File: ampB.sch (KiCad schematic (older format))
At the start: 14 parts, among them U05 Mux, U2 screw_term, U3 screw_term, U4 screw_term, U6 TL084

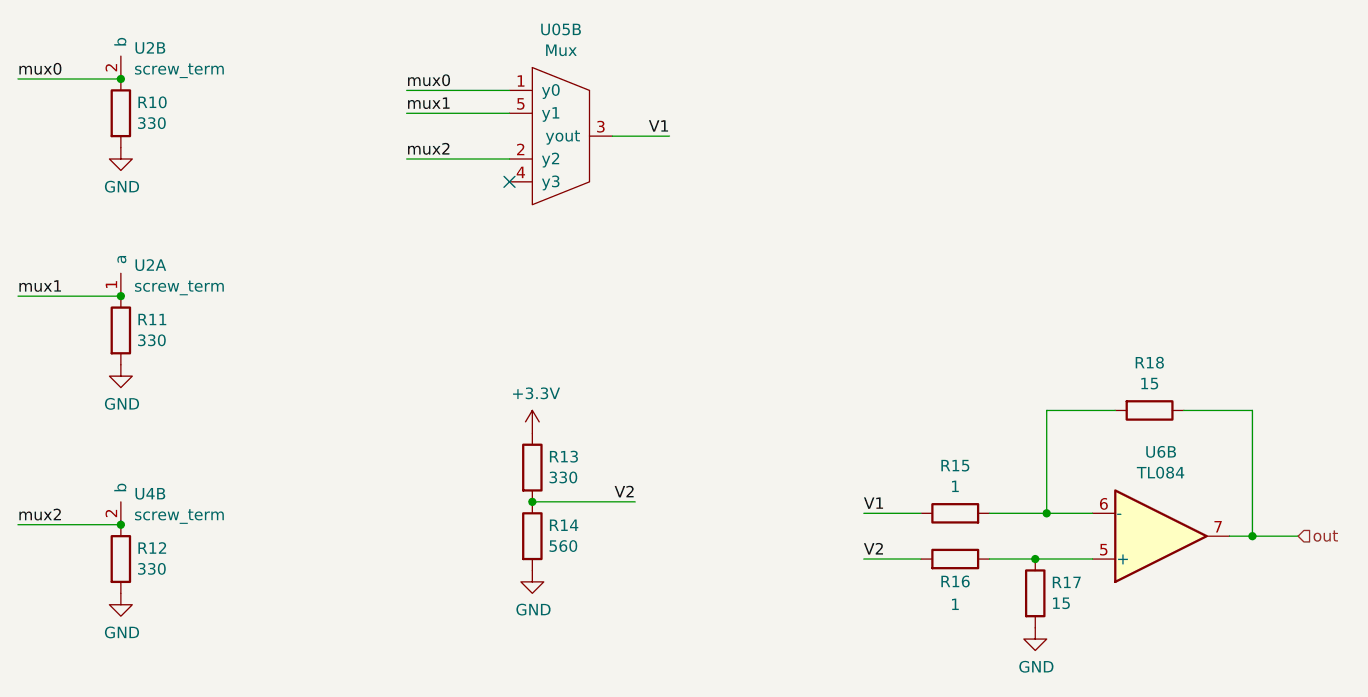
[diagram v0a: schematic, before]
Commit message: added all adc outputs
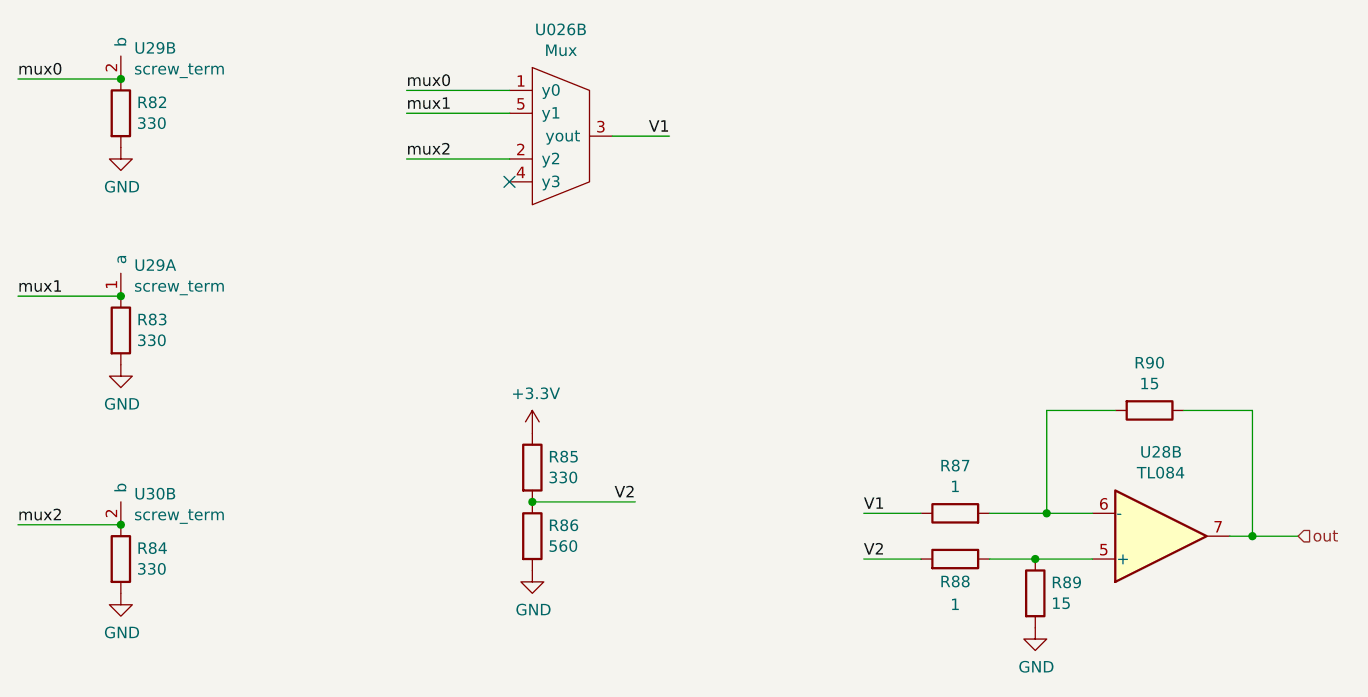
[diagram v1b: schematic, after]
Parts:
- renumbered R1 to R10, R2 to R11, R3 to R12, R4 to R13, R5 to R14, R6 to R15, R7 to R16, R8 to R17, R9 to R18, U6 to U7, U3 to U8

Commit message: added screw terminal port for sync output
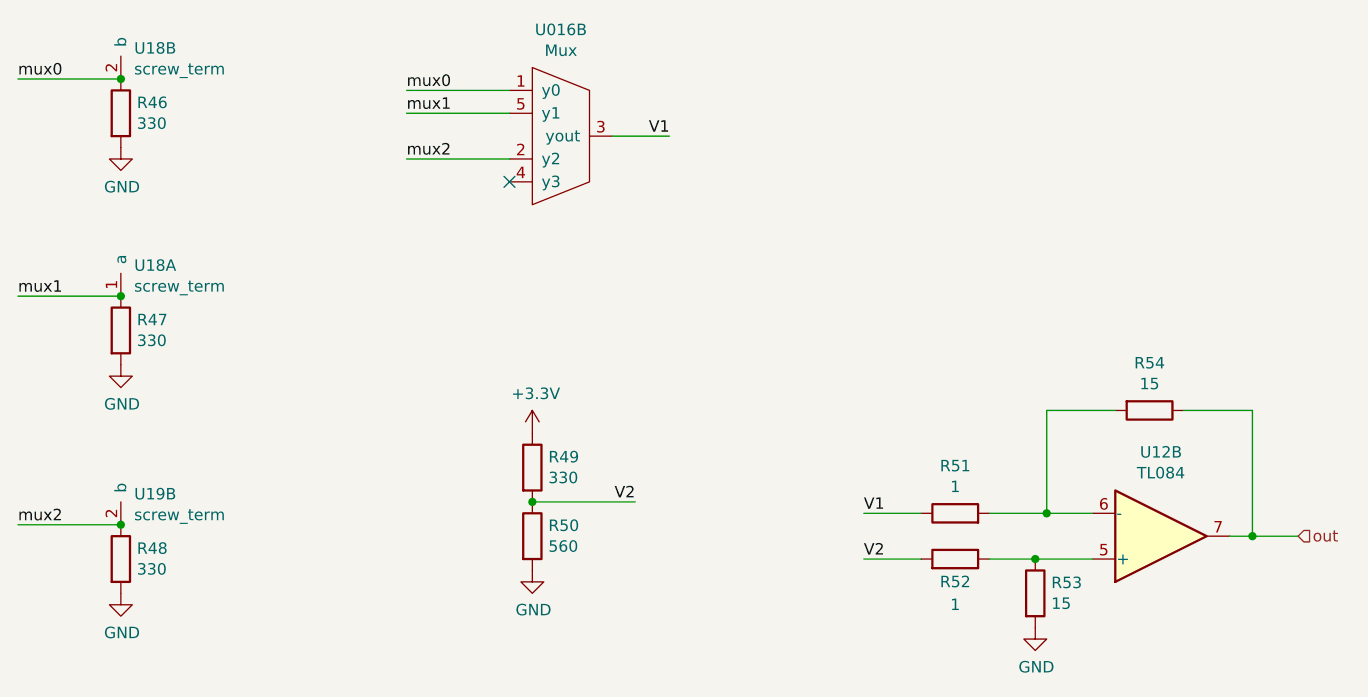
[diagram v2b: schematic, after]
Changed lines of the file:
@@
 $Descr A4 11693 8268
 encoding utf-8
-Sheet 3 11
+Sheet 7 11
 Title ""
 Date ""
@@
 AR Path="/601B4C11/6019E3AB" Ref="#PWR048"  Part="1"
 AR Path="/601B73BA/6019E3AB" Ref="#PWR078"  Part="1"
-F 0 "#PWR078" H 1450 1850 50  0001 C CNN
+F 0 "#PWR048" H 1450 1850 50  0001 C CNN
 F 1 "GND" H 1455 1927 50  0000 C CNN
 F 2 "" H 1450 2100 50  0001 C CNN
@@
 AR Path="/601B4C11/6019E3A6" Ref="U12"  Part="2"
 AR Path="/601B73BA/6019E3A6" Ref="U28"  Part="2"
-F 0 "U28" H 6000 3433 50  0000 C CNN
+F 0 "U12" H 6000 3433 50  0000 C CNN
 F 1 "TL084" H 6000 3524 50  0000 C CNN
 F 2 "" H 5950 3900 50  0001 C CNN
@@
 AR Path="/601B4C11/6019E3A5" Ref="R53"  Part="1"
 AR Path="/601B73BA/6019E3A5" Ref="R89"  Part="1"
-F 0 "R89" H 5520 4096 50  0000 L CNN
+F 0 "R53" H 5520 4096 50  0000 L CNN
 F 1 "15" H 5520 4005 50  0000 L CNN
 F 2 "Resistor_THT:R_Axial_DIN0204_L3.6mm_D1.6mm_P5.08mm_Horizontal" V 5380 4050 50  0001 C CNN
@@
 AR Path="/601B4C11/6017E430" Ref="R54"  Part="1"
 AR Path="/601B73BA/6017E430" Ref="R90"  Part="1"
-F 0 "R90" V 5743 3250 50  0000 C CNN
+F 0 "R54" V 5743 3250 50  0000 C CNN
 F 1 "15" V 5834 3250 50  0000 C CNN
 F 2 "Resistor_THT:R_Axial_DIN0204_L3.6mm_D1.6mm_P5.08mm_Horizontal" V 5880 3250 50  0001 C CNN
@@
 AR Path="/601B4C11/60198F33" Ref="R51"  Part="1"
 AR Path="/601B73BA/60198F33" Ref="R87"  Part="1"
-F 0 "R87" V 5307 3700 50  0000 C CNN
+F 0 "R51" V 5307 3700 50  0000 C CNN
 F 1 "1" V 5216 3700 50  0000 C CNN
 F 2 "Resistor_THT:R_Axial_DIN0204_L3.6mm_D1.6mm_P5.08mm_Horizontal" V 5030 3700 50  0001 C CNN
@@
 AR Path="/601B4C11/6017E432" Ref="R52"  Part="1"
 AR Path="/601B73BA/6017E432" Ref="R88"  Part="1"
-F 0 "R88" V 5000 3900 50  0000 C CNN
+F 0 "R52" V 5000 3900 50  0000 C CNN
 F 1 "1" V 4900 3900 50  0000 C CNN
 F 2 "Resistor_THT:R_Axial_DIN0204_L3.6mm_D1.6mm_P5.08mm_Horizontal" V 5030 3900 50  0001 C CNN
@@
 AR Path="/601B4C11/60198F35" Ref="R49"  Part="1"
 AR Path="/601B73BA/60198F35" Ref="R85"  Part="1"
-F 0 "R85" H 3320 3546 50  0000 L CNN
+F 0 "R49" H 3320 3546 50  0000 L CNN
 F 1 "330" H 3320 3455 50  0000 L CNN
 F 2 "Resistor_THT:R_Axial_DIN0204_L3.6mm_D1.6mm_P5.08mm_Horizontal" V 3180 3500 50  0001 C CNN
@@
 AR Path="/601B4C11/6019E3B4" Ref="R50"  Part="1"
 AR Path="/601B73BA/6019E3B4" Ref="R86"  Part="1"
-F 0 "R86" H 3320 3846 50  0000 L CNN
+F 0 "R50" H 3320 3846 50  0000 L CNN
 F 1 "560" H 3320 3755 50  0000 L CNN
 F 2 "Resistor_THT:R_Axial_DIN0204_L3.6mm_D1.6mm_P5.08mm_Horizontal" V 3180 3800 50  0001 C CNN
@@
 AR Path="/601B4C11/6019E3B5" Ref="#PWR051"  Part="1"
 AR Path="/601B73BA/6019E3B5" Ref="#PWR081"  Part="1"
-F 0 "#PWR081" H 3250 3200 50  0001 C CNN
+F 0 "#PWR051" H 3250 3200 50  0001 C CNN
 F 1 "+3.3V" H 3265 3523 50  0000 C CNN
 F 2 "" H 3250 3350 50  0001 C CNN
@@
 AR Path="/601B4C11/6017E436" Ref="#PWR052"  Part="1"
 AR Path="/601B73BA/6017E436" Ref="#PWR082"  Part="1"
-F 0 "#PWR082" H 3250 3700 50  0001 C CNN
+F 0 "#PWR052" H 3250 3700 50  0001 C CNN
 F 1 "GND" H 3255 3777 50  0000 C CNN
 F 2 "" H 3250 3950 50  0001 C CNN
@@
 AR Path="/601B4C11/6019E3AC" Ref="#PWR053"  Part="1"
 AR Path="/601B73BA/6019E3AC" Ref="#PWR083"  Part="1"
-F 0 "#PWR083" H 5450 3950 50  0001 C CNN
+F 0 "#PWR053" H 5450 3950 50  0001 C CNN
 F 1 "GND" H 5455 4027 50  0000 C CNN
 F 2 "" H 5450 4200 50  0001 C CNN
@@
 AR Path="/601B4C11/60198F2A" Ref="R46"  Part="1"
 AR Path="/601B73BA/60198F2A" Ref="R82"  Part="1"
-F 0 "R82" H 1520 1996 50  0000 L CNN
+F 0 "R46" H 1520 1996 50  0000 L CNN
 F 1 "330" H 1520 1905 50  0000 L CNN
 F 2 "Resistor_THT:R_Axial_DIN0204_L3.6mm_D1.6mm_P5.08mm_Horizontal" V 1380 1950 50  0001 C CNN
@@
 AR Path="/601B4C11/60198F2C" Ref="U016"  Part="2"
 AR Path="/601B73BA/60198F2C" Ref="U026"  Part="2"
-F 0 "U026" H 3375 2515 50  0000 C CNN
+F 0 "U016" H 3375 2515 50  0000 C CNN
 F 1 "Mux" H 3375 2424 50  0000 C CNN
 F 2 "" H 3350 2050 50  0001 C CNN
@@
 AR Path="/601B4C11/60198F2D" Ref="#PWR049"  Part="1"
 AR Path="/601B73BA/60198F2D" Ref="#PWR079"  Part="1"
-F 0 "#PWR079" H 1450 2800 50  0001 C CNN
+F 0 "#PWR049" H 1450 2800 50  0001 C CNN
 F 1 "GND" H 1455 2877 50  0000 C CNN
 F 2 "" H 1450 3050 50  0001 C CNN
@@
 AR Path="/601B4C11/6017E43C" Ref="R47"  Part="1"
 AR Path="/601B73BA/6017E43C" Ref="R83"  Part="1"
-F 0 "R83" H 1520 2946 50  0000 L CNN
+F 0 "R47" H 1520 2946 50  0000 L CNN
 F 1 "330" H 1520 2855 50  0000 L CNN
 F 2 "Resistor_THT:R_Axial_DIN0204_L3.6mm_D1.6mm_P5.08mm_Horizontal" V 1380 2900 50  0001 C CNN
@@
 AR Path="/601B4C11/60198F2E" Ref="U18"  Part="1"
 AR Path="/601B73BA/60198F2E" Ref="U29"  Part="1"
-F 0 "U29" H 1508 2884 50  0000 L CNN
+F 0 "U18" H 1508 2884 50  0000 L CNN
 F 1 "screw_term" H 1508 2793 50  0000 L CNN
 F 2 "Connector_PinHeader_1.27mm:PinHeader_1x02_P1.27mm_Vertical" H 1450 2750 50  0001 C CNN
@@
 AR Path="/601B4C11/60198F2F" Ref="#PWR050"  Part="1"
 AR Path="/601B73BA/60198F2F" Ref="#PWR080"  Part="1"
-F 0 "#PWR080" H 1450 3800 50  0001 C CNN
+F 0 "#PWR050" H 1450 3800 50  0001 C CNN
 F 1 "GND" H 1455 3877 50  0000 C CNN
 F 2 "" H 1450 4050 50  0001 C CNN
@@
 AR Path="/601B4C11/6019E3B6" Ref="R48"  Part="1"
 AR Path="/601B73BA/6019E3B6" Ref="R84"  Part="1"
-F 0 "R84" H 1520 3946 50  0000 L CNN
+F 0 "R48" H 1520 3946 50  0000 L CNN
 F 1 "330" H 1520 3855 50  0000 L CNN
 F 2 "Resistor_THT:R_Axial_DIN0204_L3.6mm_D1.6mm_P5.08mm_Horizontal" V 1380 3900 50  0001 C CNN
@@
 AR Path="/601B4C11/6019A2A3" Ref="U18"  Part="2"
 AR Path="/601B73BA/6019A2A3" Ref="U29"  Part="2"
-F 0 "U29" H 1508 1934 50  0000 L CNN
+F 0 "U18" H 1508 1934 50  0000 L CNN
 F 1 "screw_term" H 1508 1843 50  0000 L CNN
 F 2 "Connector_PinHeader_1.27mm:PinHeader_1x02_P1.27mm_Vertical" H 1450 1800 50  0001 C CNN
@@
 AR Path="/601B4C11/6019E3B8" Ref="U19"  Part="2"
 AR Path="/601B73BA/6019E3B8" Ref="U30"  Part="2"
-F 0 "U30" H 1508 3884 50  0000 L CNN
+F 0 "U19" H 1508 3884 50  0000 L CNN
 F 1 "screw_term" H 1508 3793 50  0000 L CNN
 F 2 "Connector_PinHeader_1.27mm:PinHeader_1x02_P1.27mm_Vertical" H 1450 3750 50  0001 C CNN

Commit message: annotated sync in and out
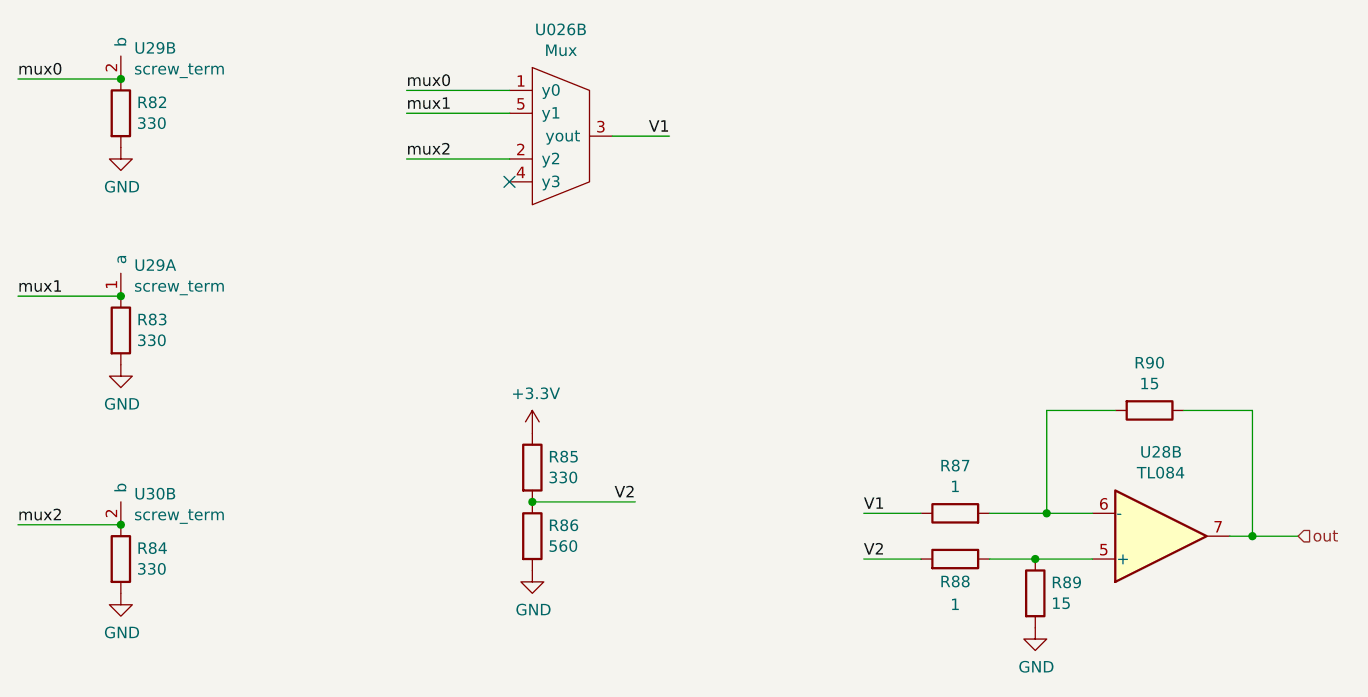
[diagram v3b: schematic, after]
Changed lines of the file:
@@
 AR Path="/601B4C11/6019E3AB" Ref="#PWR048"  Part="1"
 AR Path="/601B73BA/6019E3AB" Ref="#PWR078"  Part="1"
-F 0 "#PWR048" H 1450 1850 50  0001 C CNN
+F 0 "#PWR078" H 1450 1850 50  0001 C CNN
 F 1 "GND" H 1455 1927 50  0000 C CNN
 F 2 "" H 1450 2100 50  0001 C CNN
@@
 AR Path="/601B4C11/6019E3A6" Ref="U12"  Part="2"
 AR Path="/601B73BA/6019E3A6" Ref="U28"  Part="2"
-F 0 "U12" H 6000 3433 50  0000 C CNN
+F 0 "U28" H 6000 3433 50  0000 C CNN
 F 1 "TL084" H 6000 3524 50  0000 C CNN
 F 2 "" H 5950 3900 50  0001 C CNN
@@
 AR Path="/601B4C11/6019E3A5" Ref="R53"  Part="1"
 AR Path="/601B73BA/6019E3A5" Ref="R89"  Part="1"
-F 0 "R53" H 5520 4096 50  0000 L CNN
+F 0 "R89" H 5520 4096 50  0000 L CNN
 F 1 "15" H 5520 4005 50  0000 L CNN
 F 2 "Resistor_THT:R_Axial_DIN0204_L3.6mm_D1.6mm_P5.08mm_Horizontal" V 5380 4050 50  0001 C CNN
@@
 AR Path="/601B4C11/6017E430" Ref="R54"  Part="1"
 AR Path="/601B73BA/6017E430" Ref="R90"  Part="1"
-F 0 "R54" V 5743 3250 50  0000 C CNN
+F 0 "R90" V 5743 3250 50  0000 C CNN
 F 1 "15" V 5834 3250 50  0000 C CNN
 F 2 "Resistor_THT:R_Axial_DIN0204_L3.6mm_D1.6mm_P5.08mm_Horizontal" V 5880 3250 50  0001 C CNN
@@
 AR Path="/601B4C11/60198F33" Ref="R51"  Part="1"
 AR Path="/601B73BA/60198F33" Ref="R87"  Part="1"
-F 0 "R51" V 5307 3700 50  0000 C CNN
+F 0 "R87" V 5307 3700 50  0000 C CNN
 F 1 "1" V 5216 3700 50  0000 C CNN
 F 2 "Resistor_THT:R_Axial_DIN0204_L3.6mm_D1.6mm_P5.08mm_Horizontal" V 5030 3700 50  0001 C CNN
@@
 AR Path="/601B4C11/6017E432" Ref="R52"  Part="1"
 AR Path="/601B73BA/6017E432" Ref="R88"  Part="1"
-F 0 "R52" V 5000 3900 50  0000 C CNN
+F 0 "R88" V 5000 3900 50  0000 C CNN
 F 1 "1" V 4900 3900 50  0000 C CNN
 F 2 "Resistor_THT:R_Axial_DIN0204_L3.6mm_D1.6mm_P5.08mm_Horizontal" V 5030 3900 50  0001 C CNN
@@
 AR Path="/601B4C11/60198F35" Ref="R49"  Part="1"
 AR Path="/601B73BA/60198F35" Ref="R85"  Part="1"
-F 0 "R49" H 3320 3546 50  0000 L CNN
+F 0 "R85" H 3320 3546 50  0000 L CNN
 F 1 "330" H 3320 3455 50  0000 L CNN
 F 2 "Resistor_THT:R_Axial_DIN0204_L3.6mm_D1.6mm_P5.08mm_Horizontal" V 3180 3500 50  0001 C CNN
@@
 AR Path="/601B4C11/6019E3B4" Ref="R50"  Part="1"
 AR Path="/601B73BA/6019E3B4" Ref="R86"  Part="1"
-F 0 "R50" H 3320 3846 50  0000 L CNN
+F 0 "R86" H 3320 3846 50  0000 L CNN
 F 1 "560" H 3320 3755 50  0000 L CNN
 F 2 "Resistor_THT:R_Axial_DIN0204_L3.6mm_D1.6mm_P5.08mm_Horizontal" V 3180 3800 50  0001 C CNN
@@
 AR Path="/601B4C11/6019E3B5" Ref="#PWR051"  Part="1"
 AR Path="/601B73BA/6019E3B5" Ref="#PWR081"  Part="1"
-F 0 "#PWR051" H 3250 3200 50  0001 C CNN
+F 0 "#PWR081" H 3250 3200 50  0001 C CNN
 F 1 "+3.3V" H 3265 3523 50  0000 C CNN
 F 2 "" H 3250 3350 50  0001 C CNN
@@
 AR Path="/601B4C11/6017E436" Ref="#PWR052"  Part="1"
 AR Path="/601B73BA/6017E436" Ref="#PWR082"  Part="1"
-F 0 "#PWR052" H 3250 3700 50  0001 C CNN
+F 0 "#PWR082" H 3250 3700 50  0001 C CNN
 F 1 "GND" H 3255 3777 50  0000 C CNN
 F 2 "" H 3250 3950 50  0001 C CNN
@@
 AR Path="/601B4C11/6019E3AC" Ref="#PWR053"  Part="1"
 AR Path="/601B73BA/6019E3AC" Ref="#PWR083"  Part="1"
-F 0 "#PWR053" H 5450 3950 50  0001 C CNN
+F 0 "#PWR083" H 5450 3950 50  0001 C CNN
 F 1 "GND" H 5455 4027 50  0000 C CNN
 F 2 "" H 5450 4200 50  0001 C CNN
@@
 AR Path="/601B4C11/60198F2A" Ref="R46"  Part="1"
 AR Path="/601B73BA/60198F2A" Ref="R82"  Part="1"
-F 0 "R46" H 1520 1996 50  0000 L CNN
+F 0 "R82" H 1520 1996 50  0000 L CNN
 F 1 "330" H 1520 1905 50  0000 L CNN
 F 2 "Resistor_THT:R_Axial_DIN0204_L3.6mm_D1.6mm_P5.08mm_Horizontal" V 1380 1950 50  0001 C CNN
@@
 AR Path="/601B4C11/60198F2C" Ref="U016"  Part="2"
 AR Path="/601B73BA/60198F2C" Ref="U026"  Part="2"
-F 0 "U016" H 3375 2515 50  0000 C CNN
+F 0 "U026" H 3375 2515 50  0000 C CNN
 F 1 "Mux" H 3375 2424 50  0000 C CNN
 F 2 "" H 3350 2050 50  0001 C CNN
@@
 AR Path="/601B4C11/60198F2D" Ref="#PWR049"  Part="1"
 AR Path="/601B73BA/60198F2D" Ref="#PWR079"  Part="1"
-F 0 "#PWR049" H 1450 2800 50  0001 C CNN
+F 0 "#PWR079" H 1450 2800 50  0001 C CNN
 F 1 "GND" H 1455 2877 50  0000 C CNN
 F 2 "" H 1450 3050 50  0001 C CNN
@@
 AR Path="/601B4C11/6017E43C" Ref="R47"  Part="1"
 AR Path="/601B73BA/6017E43C" Ref="R83"  Part="1"
-F 0 "R47" H 1520 2946 50  0000 L CNN
+F 0 "R83" H 1520 2946 50  0000 L CNN
 F 1 "330" H 1520 2855 50  0000 L CNN
 F 2 "Resistor_THT:R_Axial_DIN0204_L3.6mm_D1.6mm_P5.08mm_Horizontal" V 1380 2900 50  0001 C CNN
@@
 AR Path="/601B4C11/60198F2E" Ref="U18"  Part="1"
 AR Path="/601B73BA/60198F2E" Ref="U29"  Part="1"
-F 0 "U18" H 1508 2884 50  0000 L CNN
+F 0 "U29" H 1508 2884 50  0000 L CNN
 F 1 "screw_term" H 1508 2793 50  0000 L CNN
 F 2 "Connector_PinHeader_1.27mm:PinHeader_1x02_P1.27mm_Vertical" H 1450 2750 50  0001 C CNN
@@
 AR Path="/601B4C11/60198F2F" Ref="#PWR050"  Part="1"
 AR Path="/601B73BA/60198F2F" Ref="#PWR080"  Part="1"
-F 0 "#PWR050" H 1450 3800 50  0001 C CNN
+F 0 "#PWR080" H 1450 3800 50  0001 C CNN
 F 1 "GND" H 1455 3877 50  0000 C CNN
 F 2 "" H 1450 4050 50  0001 C CNN
@@
 AR Path="/601B4C11/6019E3B6" Ref="R48"  Part="1"
 AR Path="/601B73BA/6019E3B6" Ref="R84"  Part="1"
-F 0 "R48" H 1520 3946 50  0000 L CNN
+F 0 "R84" H 1520 3946 50  0000 L CNN
 F 1 "330" H 1520 3855 50  0000 L CNN
 F 2 "Resistor_THT:R_Axial_DIN0204_L3.6mm_D1.6mm_P5.08mm_Horizontal" V 1380 3900 50  0001 C CNN
@@
 AR Path="/601B4C11/6019A2A3" Ref="U18"  Part="2"
 AR Path="/601B73BA/6019A2A3" Ref="U29"  Part="2"
-F 0 "U18" H 1508 1934 50  0000 L CNN
+F 0 "U29" H 1508 1934 50  0000 L CNN
 F 1 "screw_term" H 1508 1843 50  0000 L CNN
 F 2 "Connector_PinHeader_1.27mm:PinHeader_1x02_P1.27mm_Vertical" H 1450 1800 50  0001 C CNN
@@
 AR Path="/601B4C11/6019E3B8" Ref="U19"  Part="2"
 AR Path="/601B73BA/6019E3B8" Ref="U30"  Part="2"
-F 0 "U19" H 1508 3884 50  0000 L CNN
+F 0 "U30" H 1508 3884 50  0000 L CNN
 F 1 "screw_term" H 1508 3793 50  0000 L CNN
 F 2 "Connector_PinHeader_1.27mm:PinHeader_1x02_P1.27mm_Vertical" H 1450 3750 50  0001 C CNN

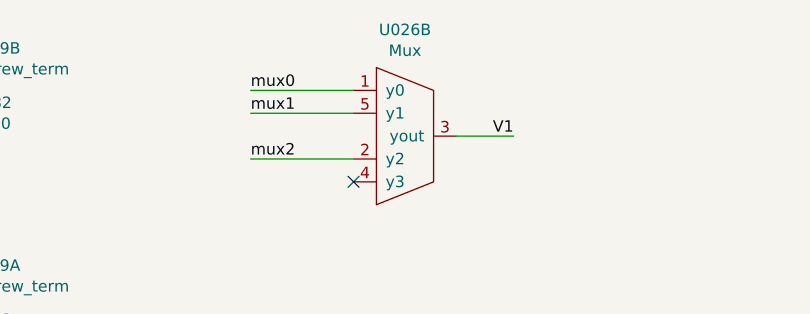
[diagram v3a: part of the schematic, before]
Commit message: added no connects on teensy
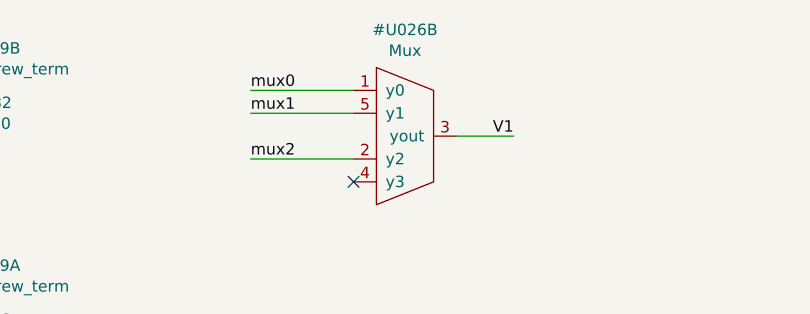
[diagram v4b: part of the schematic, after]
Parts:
- removed U05: Mux, symbol PNG_PCB_Parts:Mux
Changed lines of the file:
@@
 AR Path="/6017CC5E/60198F2C" Ref="U?"  Part="1"
 AR Path="/6017DA21/60198F2C" Ref="U?"  Part="1"
-AR Path="/601927EB/60198F2C" Ref="U05"  Part="2"
+AR Path="/601927EB/60198F2C" Ref="#U05"  Part="2"
 AR Path="/6019DBCE/60198F2C" Ref="U?"  Part="2"
-AR Path="/601B4C11/60198F2C" Ref="U016"  Part="2"
-AR Path="/601B73BA/60198F2C" Ref="U026"  Part="2"
-F 0 "U026" H 3375 2515 50  0000 C CNN
+AR Path="/601B4C11/60198F2C" Ref="#U016"  Part="2"
+AR Path="/601B73BA/60198F2C" Ref="#U026"  Part="2"
+F 0 "#U026" H 3375 2515 50  0000 C CNN
 F 1 "Mux" H 3375 2424 50  0000 C CNN
 F 2 "" H 3350 2050 50  0001 C CNN
